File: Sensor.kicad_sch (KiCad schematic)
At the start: 13 parts, among them J2 Enc1, J3 Enc3, J4 Enc2, J5 Enc4

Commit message: 回路図の作成
完成が見えてきた
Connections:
- net Lim_Mode renamed Limit_Mode
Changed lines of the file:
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@@
 		)
 	)
-	(hierarchical_label "Lim_Mode"
+	(hierarchical_label "Limit_Mode"
 		(shape input)
 		(at 165.1 49.53 0)

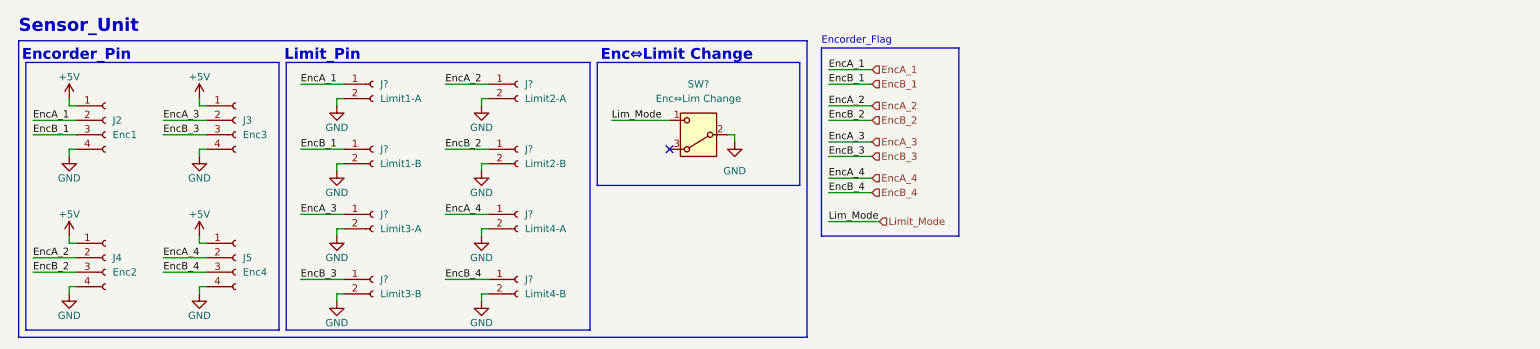
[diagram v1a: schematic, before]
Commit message: 回路図9割完成
回路図は9割完成
次からは配線作業をする
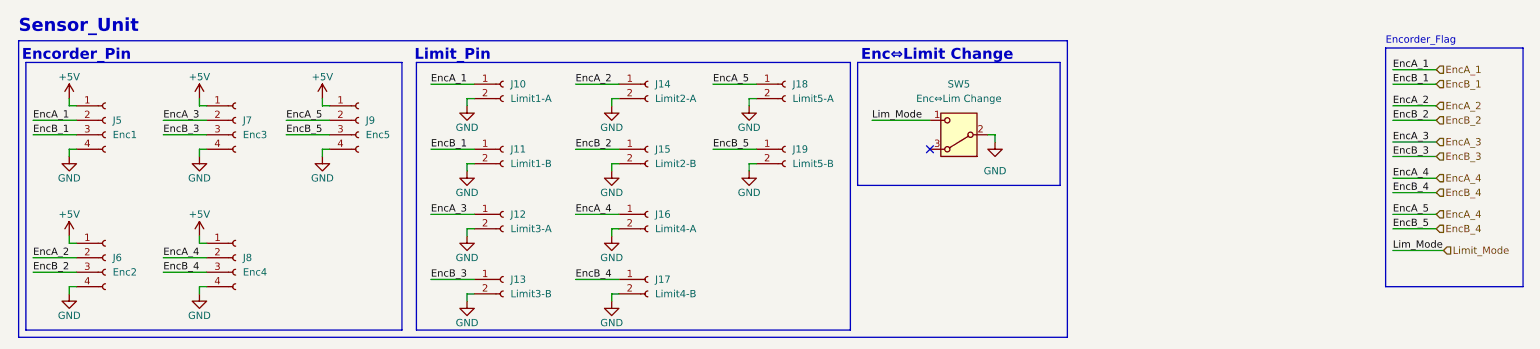
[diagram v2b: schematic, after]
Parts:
- added J18: Limit5-A, Connector_JST:JST_XA_B02B-XASK-1_1x02_P2.50mm_Vertical, symbol Connector:Conn_01x02_Socket
- added J19: Limit5-B, Connector_JST:JST_XA_B02B-XASK-1_1x02_P2.50mm_Vertical, symbol Connector:Conn_01x02_Socket
- added J9: Enc5, Connector_JST:JST_XA_S04B-XASK-1_1x04_P2.50mm_Horizontal, symbol Connector:Conn_01x04_Socket
- gave numbers to parts that had none: 9
- renumbered J2 to J5, J4 to J6, J3 to J7, J5 to J8
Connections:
- net +5V: now also J9.1 (Pin_1)
- net EncA_4: now also J18.1 (Pin_1), J9.2 (Pin_2)
- net EncB_4: now also J19.1 (Pin_1), J9.3 (Pin_3)
- net GND: now also J18.2 (Pin_2), J19.2 (Pin_2), J9.4 (Pin_4)
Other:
- moved on the sheet: J10, J11, J12, J13, J14, J15, J16, J17, SW5

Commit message: 回路図作った
リミットとエンコ共存いやかも
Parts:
- removed J10: Limit1-A, Connector_JST:JST_XA_B02B-XASK-1_1x02_P2.50mm_Vertical, symbol Connector:Conn_01x02_Socket
- removed J11: Limit1-B, Connector_JST:JST_XA_B02B-XASK-1_1x02_P2.50mm_Vertical, symbol Connector:Conn_01x02_Socket
- removed J12: Limit3-A, Connector_JST:JST_XA_B02B-XASK-1_1x02_P2.50mm_Vertical, symbol Connector:Conn_01x02_Socket
- removed J13: Limit3-B, Connector_JST:JST_XA_B02B-XASK-1_1x02_P2.50mm_Vertical, symbol Connector:Conn_01x02_Socket
- removed J14: Limit2-A, Connector_JST:JST_XA_B02B-XASK-1_1x02_P2.50mm_Vertical, symbol Connector:Conn_01x02_Socket
- removed J15: Limit2-B, Connector_JST:JST_XA_B02B-XASK-1_1x02_P2.50mm_Vertical, symbol Connector:Conn_01x02_Socket
- removed J16: Limit4-A, Connector_JST:JST_XA_B02B-XASK-1_1x02_P2.50mm_Vertical, symbol Connector:Conn_01x02_Socket
- removed J17: Limit4-B, Connector_JST:JST_XA_B02B-XASK-1_1x02_P2.50mm_Vertical, symbol Connector:Conn_01x02_Socket
- removed J18: Limit5-A, Connector_JST:JST_XA_B02B-XASK-1_1x02_P2.50mm_Vertical, symbol Connector:Conn_01x02_Socket
- removed J19: Limit5-B, Connector_JST:JST_XA_B02B-XASK-1_1x02_P2.50mm_Vertical, symbol Connector:Conn_01x02_Socket
- removed J5: Enc1, Connector_JST:JST_XA_S04B-XASK-1_1x04_P2.50mm_Horizontal, symbol Connector:Conn_01x04_Socket
- removed J6: Enc2, Connector_JST:JST_XA_S04B-XASK-1_1x04_P2.50mm_Horizontal, symbol Connector:Conn_01x04_Socket
- removed J7: Enc3, Connector_JST:JST_XA_S04B-XASK-1_1x04_P2.50mm_Horizontal, symbol Connector:Conn_01x04_Socket
- removed J8: Enc4, Connector_JST:JST_XA_S04B-XASK-1_1x04_P2.50mm_Horizontal, symbol Connector:Conn_01x04_Socket
- removed J9: Enc5, Connector_JST:JST_XA_S04B-XASK-1_1x04_P2.50mm_Horizontal, symbol Connector:Conn_01x04_Socket
- removed SW5: Enc⇔Lim Change, Connector_PinHeader_2.54mm:PinHeader_1x03_P2.54mm_Vertical, symbol Switch:SW_Nidec_CAS-120A1
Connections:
- no-connect marks 1 -> 0
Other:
- note removed: "Encorder_Pin"
- note removed: "Enc⇔Limit Change"
- note removed: "Limit_Pin"
- note removed: "Sensor_Unit"
